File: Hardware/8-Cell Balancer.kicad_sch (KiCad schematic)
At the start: 24 parts, among them J1 Balance, J2 SWD, SW1 Reset, SW2 Button, U1 AP7370, U2 74HC4051, U3 74HC4051, U4 NINA-B306

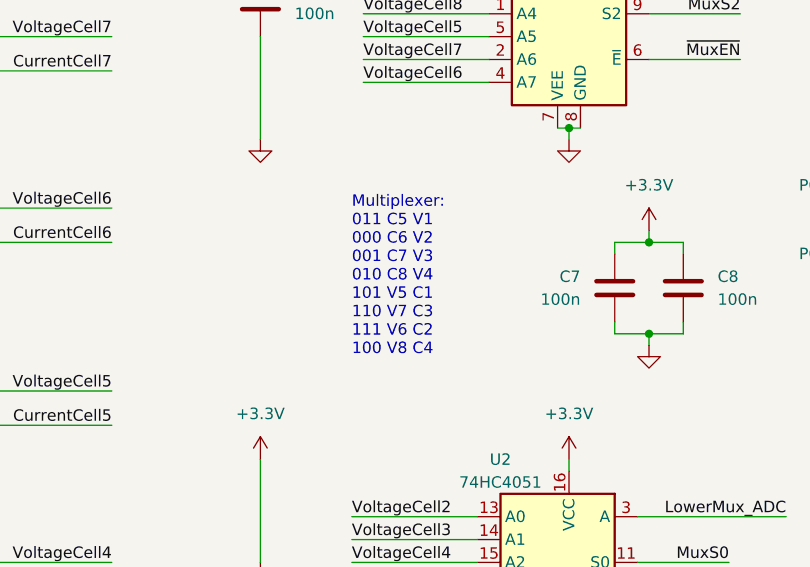
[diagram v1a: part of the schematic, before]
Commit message: schematic error correction
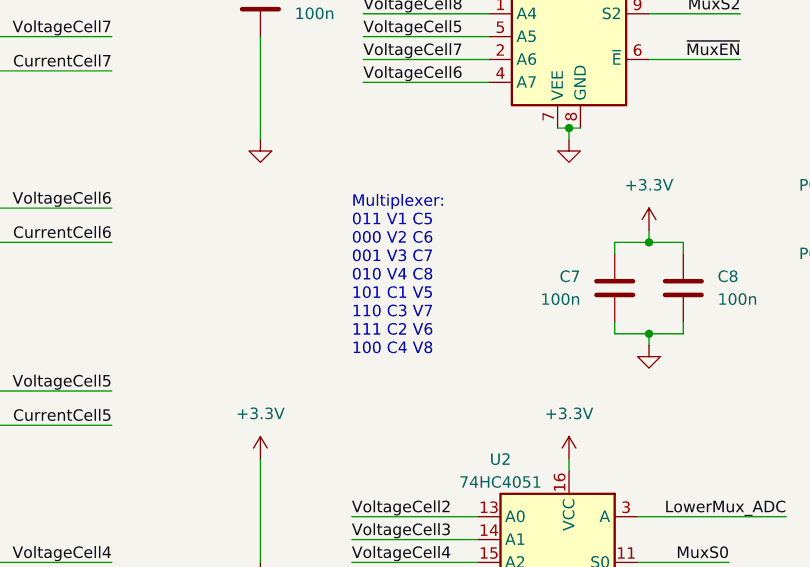
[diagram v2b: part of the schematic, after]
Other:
- note added: "Multiplexer: 011 V1 C5 000 V2 C6 001 V3 C7 010 V4 C8 101 C1 V5 110 C3 V7 111 C2 V6 100 C4 V8"
- note removed: "Multiplexer: 011 C5 V1 000 C6 V2 001 C7 V3 010 C8 V4 101 V5 C1 110 V7 C3 111 V6 C2 100 V8 C4"
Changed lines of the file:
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@@
     (effects (font (size 1.27 1.27)) (justify left bottom))
   )
-  (text "Multiplexer:\n011 C5 V1\n000 C6 V2\n001 C7 V3\n010 C8 V4\n101 V5 C1\n110 V7 C3\n111 V6 C2\n100 V8 C4"
+  (text "Multiplexer:\n011 V1 C5\n000 V2 C6\n001 V3 C7\n010 V4 C8\n101 C1 V5\n110 C3 V7\n111 C2 V6\n100 C4 V8"
     (at 143.51 76.2 0)
     (effects (font (size 1.27 1.27)) (justify left bottom))

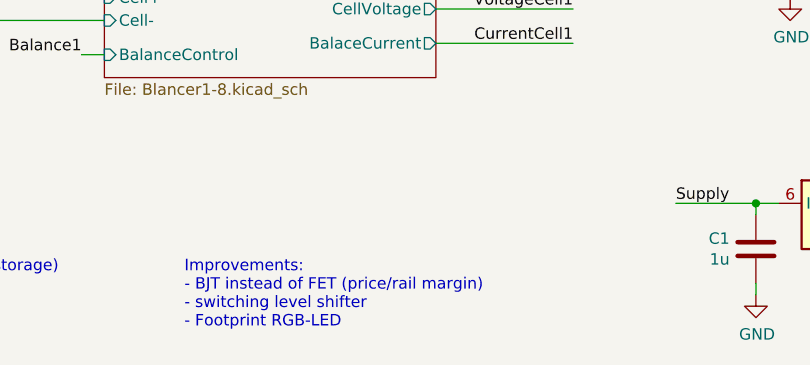
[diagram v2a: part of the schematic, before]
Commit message: hardware: update to KiCad 7
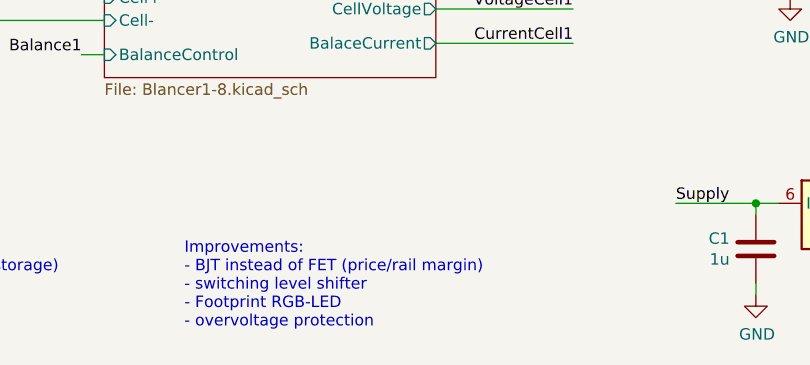
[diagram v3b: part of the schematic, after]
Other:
- note added: "Improvements: - BJT instead of FET (price/rail margin) - switching level shifter - Footprint RGB-LED - overvoltage protection"
- note removed: "Improvements: - BJT instead of FET (price/rail margin) - switching level shifter - Footprint RGB-LED"

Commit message: hardware: version 1
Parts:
- added FID1, FID2, FID3, FID4: Fiducial, Fiducial:Fiducial_1mm_Mask2mm, symbol Mechanical:Fiducial
- C1, C2: footprint Capacitor_SMD:C_0402_1005Metric -> Capacitor_SMD:C_0603_1608Metric; Mfr. Part# (none) -> GRT188R61H105KE13D; Mouser Part# (none) -> 81-GRT188R61H105KE3D
- C3, C4, C5, C6, C7, C8: Mfr. Part# (none) -> GRM155R71C104KA88D; Mouser Part# (none) -> 81-GRM155R71C104KA88
- D1: Mfr. Part# (none) -> UHD1110-FKA-CL1A13r3q1BBQFMF3; Mouser Part# (none) -> 941-UHD0FKAC11BQFMF3
- R1, R2: value 47k -> 22k; Mfr. Part# (none) -> RC0402FR-0722KL; Mouser Part# (none) -> 603-RC0402FR-0722KL
- R3, R4, R5: Mfr. Part# (none) -> RC0402FR-07620RL; Mouser Part# (none) -> 603-RC0402FR-07620RL
- SW1: value Reset -> B3U-1000; Mfr. Part# (none) -> B3U-1000P-B; Mouser Part# (none) -> 653-B3U-1000P-B
- SW2: value Button -> B3U-1000; Mfr. Part# (none) -> B3U-1000P-B; Mouser Part# (none) -> 653-B3U-1000P-B
- U1: Mfr. Part# (none) -> AP7370-33FDC-7; Mouser Part# (none) -> 621-AP7370-33FDC-7
- U2, U3: Mfr. Part# (none) -> 74LV4051BQ,115; Mouser Part# (none) -> 771-LV4051BQ115
- U4: Mfr. Part# (none) -> NINA-B306-00B; Mouser Part# (none) -> 377-NINA-B306-00B
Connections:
- net RX: now also J2.5 (Pin_5); no longer J2.6 (Pin_6)
- net TX: now also J2.6 (Pin_6); no longer J2.5 (Pin_5)
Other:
- note added: "Improvements:"
- note removed: "Improvements: - BJT instead of FET (price/rail margin) - switching level shifter - Footprint RGB-LED - overvoltage protection"
- moved on the sheet: SW1, SW2
